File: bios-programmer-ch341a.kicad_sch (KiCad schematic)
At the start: 28 parts, among them J1 USB_B_Micro, J2 SPI Debug, J3 I²C Debug, J4 +Banana+, J5 -Banana-, J6 ZIF16, SW1 RESET, U1 CH341A, U2 ISO6741, U3 ADUM1252, Y1 12M

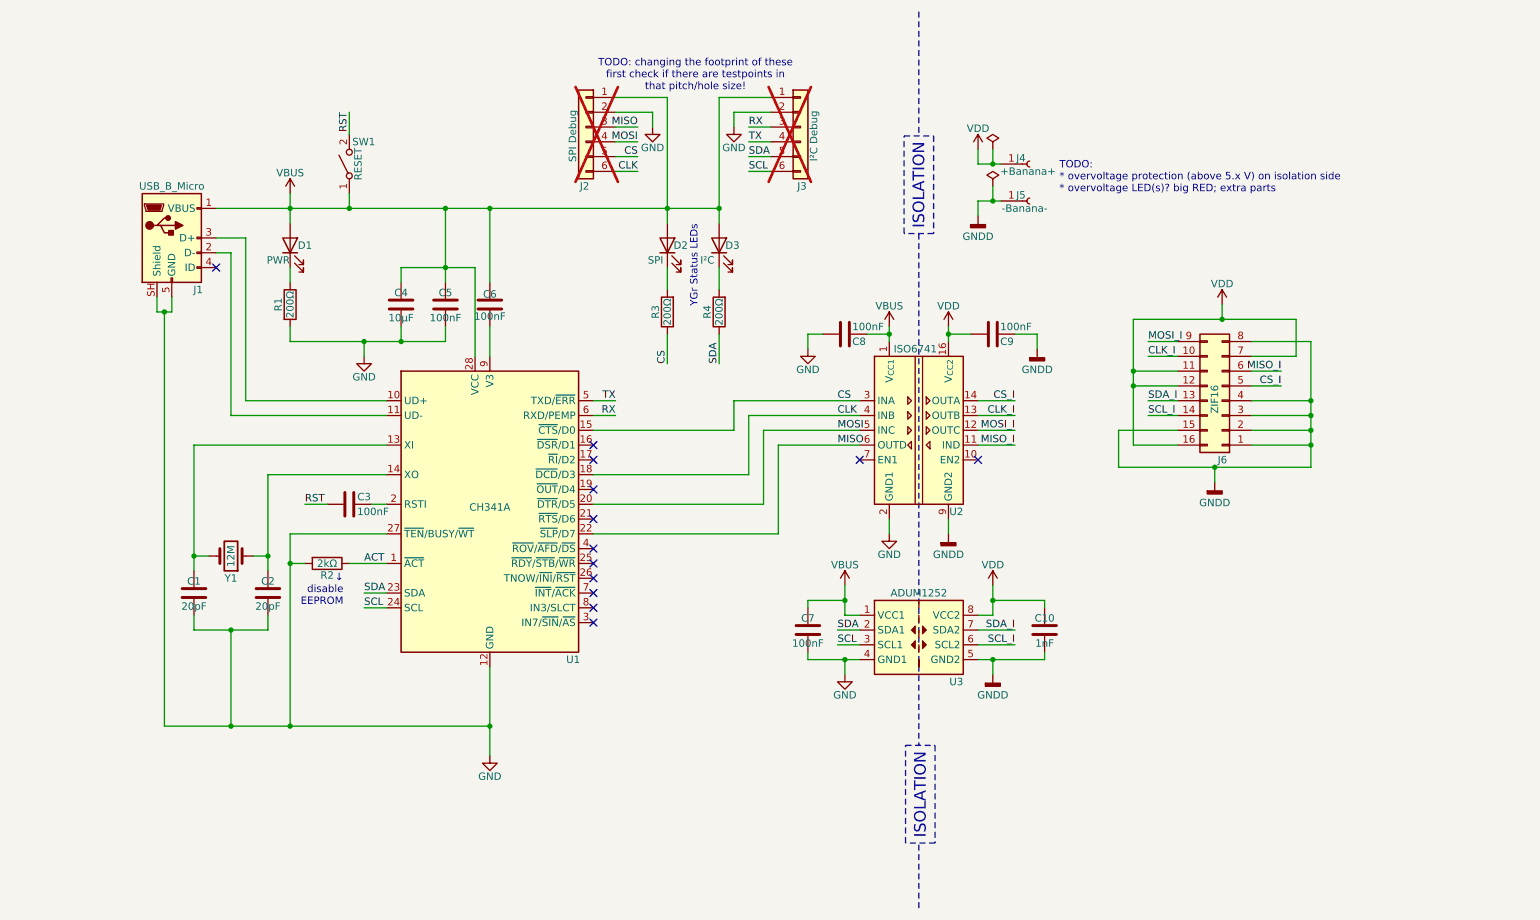
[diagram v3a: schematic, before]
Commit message: IDC connector on the bottom as standoffs and permanent programming connector
The idea is that a chip can be programmed through the ZIF socket or by connect-
ing a cable with a in-place programming clip.

This may however lead to issues and in hindsight it might become a questionable
decision: the high-speed signals will be branched and lead nowhere, which may
lead to reflections and thus signal integrity failure.

The cheap CH341 programmers do not use separate IDC connectors but instead
use the ZIF socket and a IDC adapter. This does prevent possible signal
integrity issues at the cost of an ugly adapter which doesn't prevent mis-
alignment.
If I choose to go this route myself I will have to create a better adapter
that doesn't have this problem.
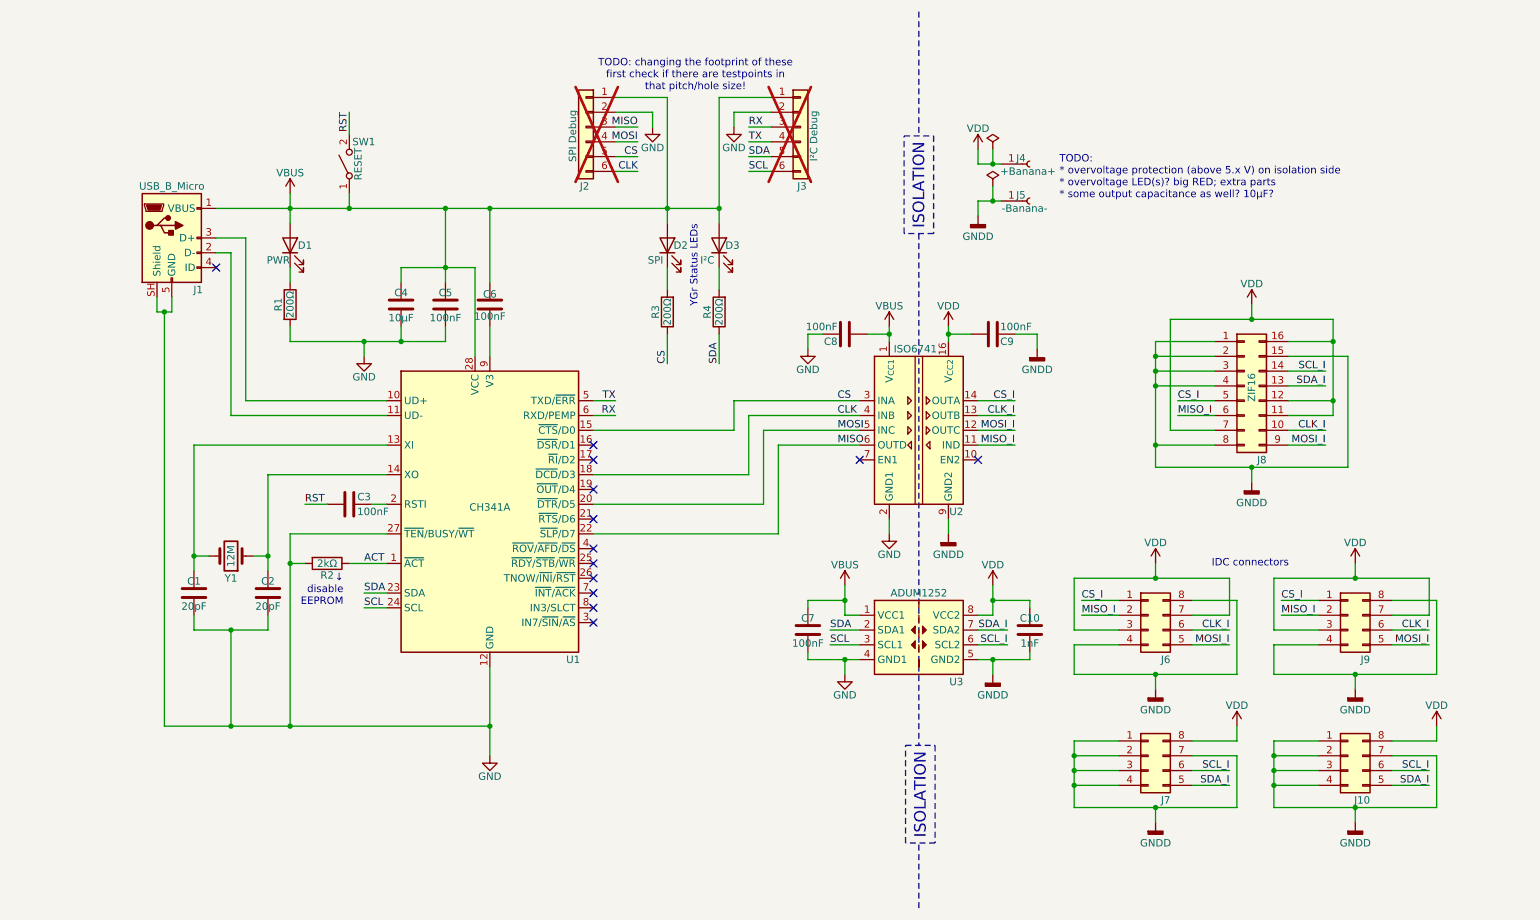
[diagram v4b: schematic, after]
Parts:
- added J10, J6, J7, J9: Conn_02x04_Counter_Clockwise, Connector_IDC:IDC-Header_2x04_P2.54mm_Horizontal, symbol Connector_Generic:Conn_02x04_Counter_Clockwise
- renumbered J6 to J8
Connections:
- net CLK_I: now also J6.6 (Pin_6), J9.6 (Pin_6)
- net CS_I: now also J6.1 (Pin_1), J9.1 (Pin_1)
- net GNDD: now also J10.1 (Pin_1), J10.2 (Pin_2), J10.3 (Pin_3), J10.4 (Pin_4), J10.7 (Pin_7), J6.4 (Pin_4), J6.8 (Pin_8), J7.1 (Pin_1), J7.2 (Pin_2), J7.3 (Pin_3), J7.4 (Pin_4), J7.7 (Pin_7), J9.4 (Pin_4), J9.8 (Pin_8)
- net MISO_I: now also J6.2 (Pin_2), J9.2 (Pin_2)
- net MOSI_I: now also J6.5 (Pin_5), J9.5 (Pin_5)
- net SCL_I: now also J10.6 (Pin_6), J7.6 (Pin_6)
- net SDA_I: now also J10.5 (Pin_5), J7.5 (Pin_5)
- net VDD: now also J10.8 (Pin_8), J6.3 (Pin_3), J6.7 (Pin_7), J7.8 (Pin_8), J9.3 (Pin_3), J9.7 (Pin_7)
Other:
- note added: "IDC connectors"
- note added: "TODO: * overvoltage protection (above 5.x V) on isolation side * overvoltage LED(s)? big RED; extra parts * some output capacitance as well? 10µF?"
- note removed: "TODO: * overvoltage protection (above 5.x V) on isolation side * overvoltage LED(s)? big RED; extra parts"
- moved on the sheet: C10, J8

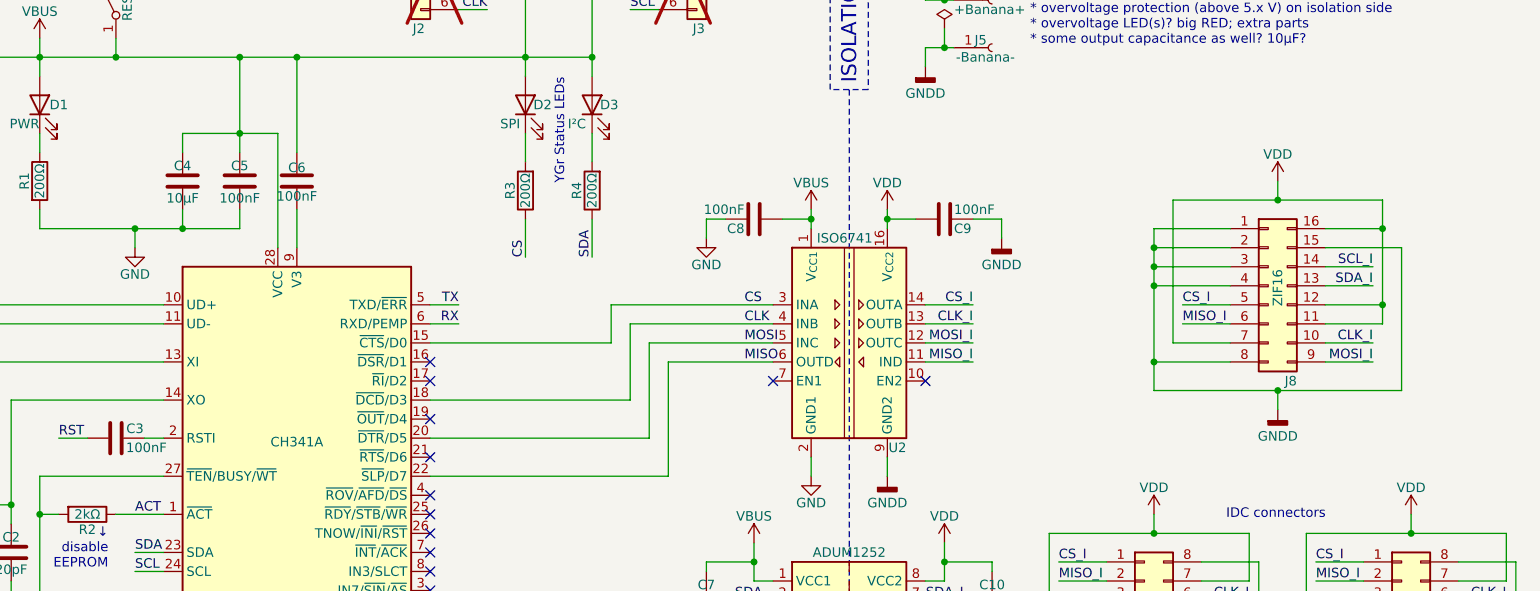
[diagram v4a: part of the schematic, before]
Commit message: First layout test & opt for 2 IPC connectors instead of 4
This layout is very preliminary and I'm committing this because I want to try
out a different layout.

Using 2 IPC connectors is probably best:
* still provides support when used diagonally - at least I expect them to
* no branching of signals, just one long string crossing THROUGH the ZIF socket

Note that I'm having some troubles with the USB connection, D+ & D- are in the
wrong way to link directly to the CH341a when used on the same side.
So either I need to find a Micro USB B with through hole signal connections,
or I need to cross them by using an extra pair of vias.
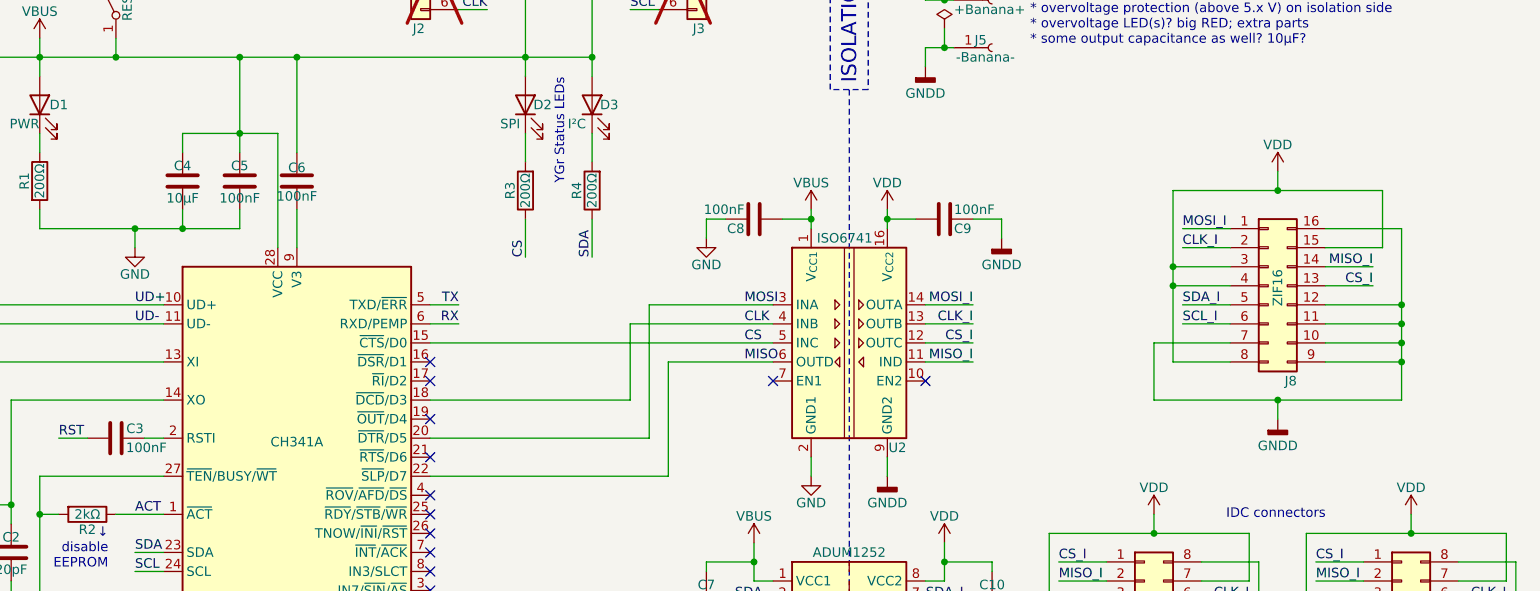
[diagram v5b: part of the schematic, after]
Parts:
- J1: footprint Connector_USB:USB_Micro-B_Amphenol_10118193-0001LF_Horizontal -> Connector_USB:USB_Micro-B_GCT_USB3076-30-A
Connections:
- net CLK_I: now also J8.2 (Pin_2); no longer J8.10 (Pin_10)
- net CS: now also U2.5 (INC); no longer U2.3 (INA)
- net CS_I: now also J8.13 (Pin_13), U2.12 (OUTC); no longer J8.5 (Pin_5), U2.14 (OUTA)
- net GNDD: now also J8.10 (Pin_10), J8.11 (Pin_11), J8.12 (Pin_12), J8.16 (Pin_16), J8.7 (Pin_7), J8.9 (Pin_9); no longer J8.1 (Pin_1), J8.15 (Pin_15), J8.2 (Pin_2), J8.3 (Pin_3), J8.4 (Pin_4), J8.8 (Pin_8)
- net MISO_I: now also J8.14 (Pin_14); no longer J8.6 (Pin_6)
- net MOSI: now also U2.3 (INA); no longer U2.5 (INC)
- net MOSI_I: now also J8.1 (Pin_1), U2.14 (OUTA); no longer J8.9 (Pin_9), U2.12 (OUTC)
- net SCL_I: now also J8.6 (Pin_6); no longer J8.14 (Pin_14)
- net SDA_I: now also J8.5 (Pin_5); no longer J8.13 (Pin_13)
- net VDD: now also J8.15 (Pin_15), J8.3 (Pin_3), J8.4 (Pin_4), J8.8 (Pin_8); no longer J8.11 (Pin_11), J8.12 (Pin_12), J8.16 (Pin_16), J8.7 (Pin_7)
- net UD-: now reaches J1.2 (D-), U1.11 (UD-)
- net UD+: now reaches J1.3 (D+), U1.10 (UD+)

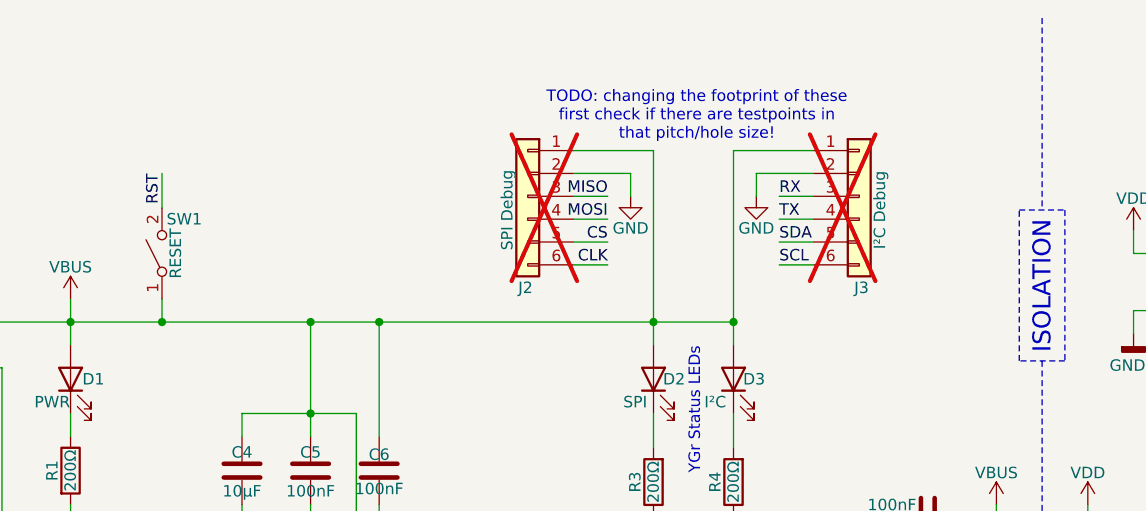
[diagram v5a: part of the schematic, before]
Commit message: PCB redesign, reducing footprint & optimizing layout
IMPORTANT: I've switched up the footprint of the ZIF socket (will require
doublechecking) in order to improve the routing.

All in all I'm pretty content with this layout idea, routing goes well and most
of the important parts have been routed in this example.

However, due to the orientation of the CH341 it will be difficult to route the
USB data signals. Since these are high-speed - the highest of all signals on
this board - it is imperative that these are routed better. On top of that it's
good to route these within a grounded channel.

Then the test headers...they have been giving me trouble. In fact that's the
reason I rotated the CH341 chip, but it seems I have create issues I cannot
solve. Thus back to the drawing board. Also, I turned the test headers into
2x03 headers. It's a bit easier to route.

Note: the off-the-shelf programmers have an outer ground ring to prevent some
interference. While I consider the validity of this in this specific design, I
intend to do something alike. However, considering the isolated design I'm not
sure this will be effective at all.
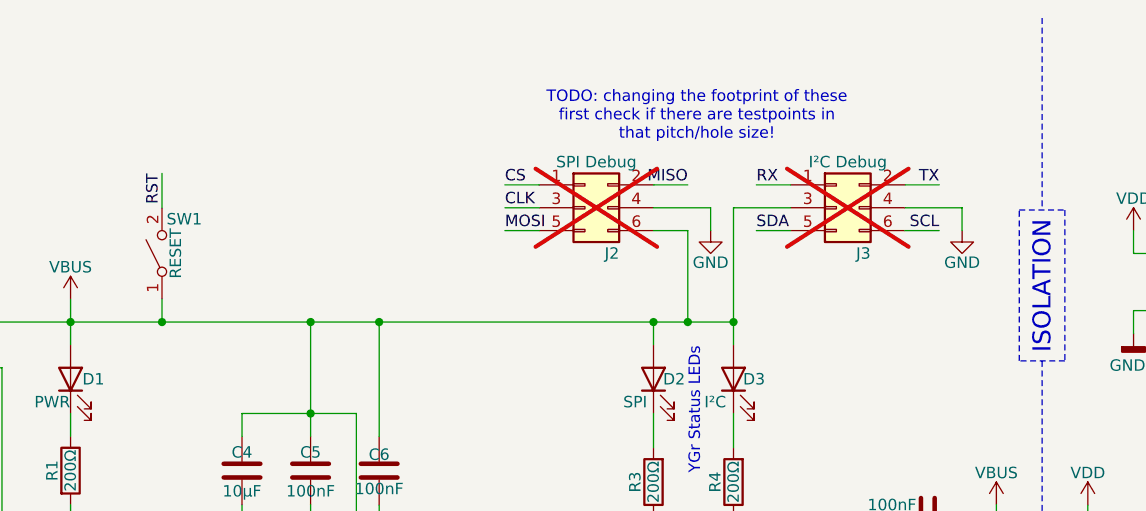
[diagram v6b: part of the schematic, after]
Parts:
- removed J2: SPI Debug, Connector_PinSocket_2.54mm:PinSocket_1x06_P2.54mm_Vertical, symbol Connector_Generic:Conn_01x06
- removed J3: I²C Debug, Connector_PinSocket_2.54mm:PinSocket_1x06_P2.54mm_Vertical, symbol Connector_Generic:Conn_01x06
- added J2: SPI Debug, Connector_PinHeader_2.54mm:PinHeader_2x03_P2.54mm_Vertical, symbol Connector_Generic:Conn_02x03_Odd_Even
- added J3: I²C Debug, Connector_PinHeader_2.54mm:PinHeader_2x03_P2.54mm_Vertical, symbol Connector_Generic:Conn_02x03_Odd_Even
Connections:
- net CLK: now also J2.3 (Pin_3)
- net CS: now also J2.1 (Pin_1)
- net GND: now also J2.4 (Pin_4), J3.4 (Pin_4)
- net MISO: now also J2.2 (Pin_2)
- net MOSI: now also J2.5 (Pin_5)
- net RX: now also J3.1 (Pin_1)
- net SCL: now also J3.6 (Pin_6)
- net SDA: now also J3.5 (Pin_5)
- net TX: now also J3.2 (Pin_2)
- net VBUS: now also J2.6 (Pin_6), J3.3 (Pin_3)

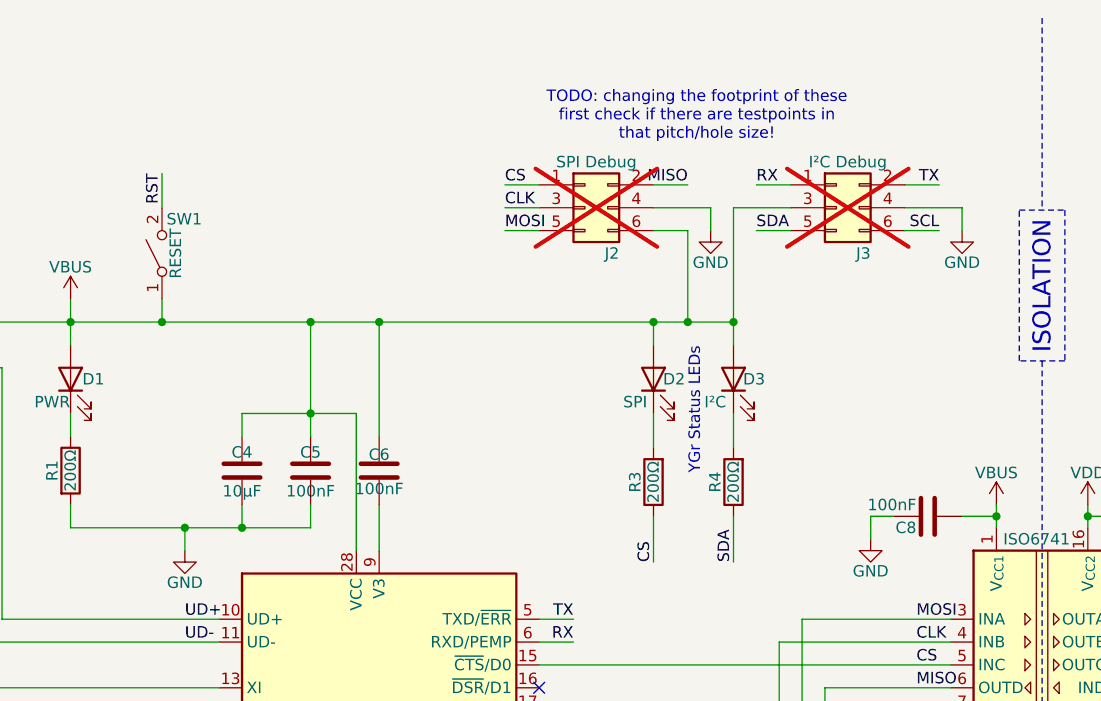
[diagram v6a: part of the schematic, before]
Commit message: PCB: reset button & ACT pulldown
Pulling down ACT (throught a resistor) disables the CH341 EEPROM check to find
its configuration. Only programmatic configuration is supported in order to
switch from SPI to I2C and vice versa.

PROBLEM: while checking the PCB I noticed that the ZIF socket - for which I've
changed the signal order - isn't correct. Or technically it is, it's just
upside down. However, it would be nicer to have pin 1 of the zif socket be
pin 1 of the (first of two) memory chips.
Changing this will change a lot of the signals coming from the isolators and
going towards the IDC connectors.
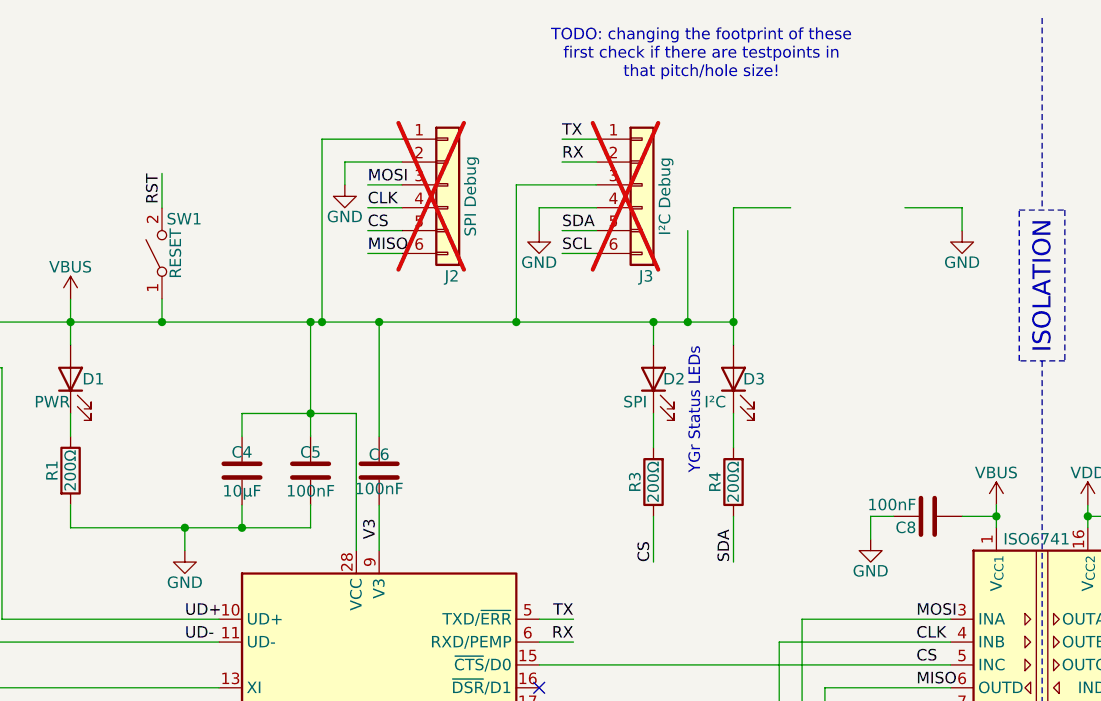
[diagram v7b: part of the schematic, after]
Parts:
- removed J2: SPI Debug, Connector_PinHeader_2.54mm:PinHeader_2x03_P2.54mm_Vertical, symbol Connector_Generic:Conn_02x03_Odd_Even
- removed J3: I²C Debug, Connector_PinHeader_2.54mm:PinHeader_2x03_P2.54mm_Vertical, symbol Connector_Generic:Conn_02x03_Odd_Even
- added J2: SPI Debug, Connector_PinSocket_1.27mm:PinSocket_1x06_P1.27mm_Vertical, symbol Connector_Generic:Conn_01x06
- added J3: I²C Debug, Connector_PinSocket_1.27mm:PinSocket_1x06_P1.27mm_Vertical, symbol Connector_Generic:Conn_01x06
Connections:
- net CLK: now also J2.4 (Pin_4)
- net CS: now also J2.5 (Pin_5)
- net GND: now also J2.2 (Pin_2), J3.4 (Pin_4)
- net MISO: now also J2.6 (Pin_6)
- net MOSI: now also J2.3 (Pin_3)
- net RX: now also J3.2 (Pin_2)
- net SCL: now also J3.6 (Pin_6)
- net SDA: now also J3.5 (Pin_5)
- net TX: now also J3.1 (Pin_1)
- net VBUS: now also J2.1 (Pin_1), J3.3 (Pin_3)
- net V3: now reaches C6.2, U1.9 (V3)
